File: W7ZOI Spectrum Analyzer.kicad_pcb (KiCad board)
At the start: 2 copper layers, 107.9 x 90.4 mm, 57 parts, among them J402 Jack-DC, J404 Jack-DC, J8 Conn_Coaxial, J9 Conn_Coaxial, U401 LM358, U402 LM358, U403 LM358

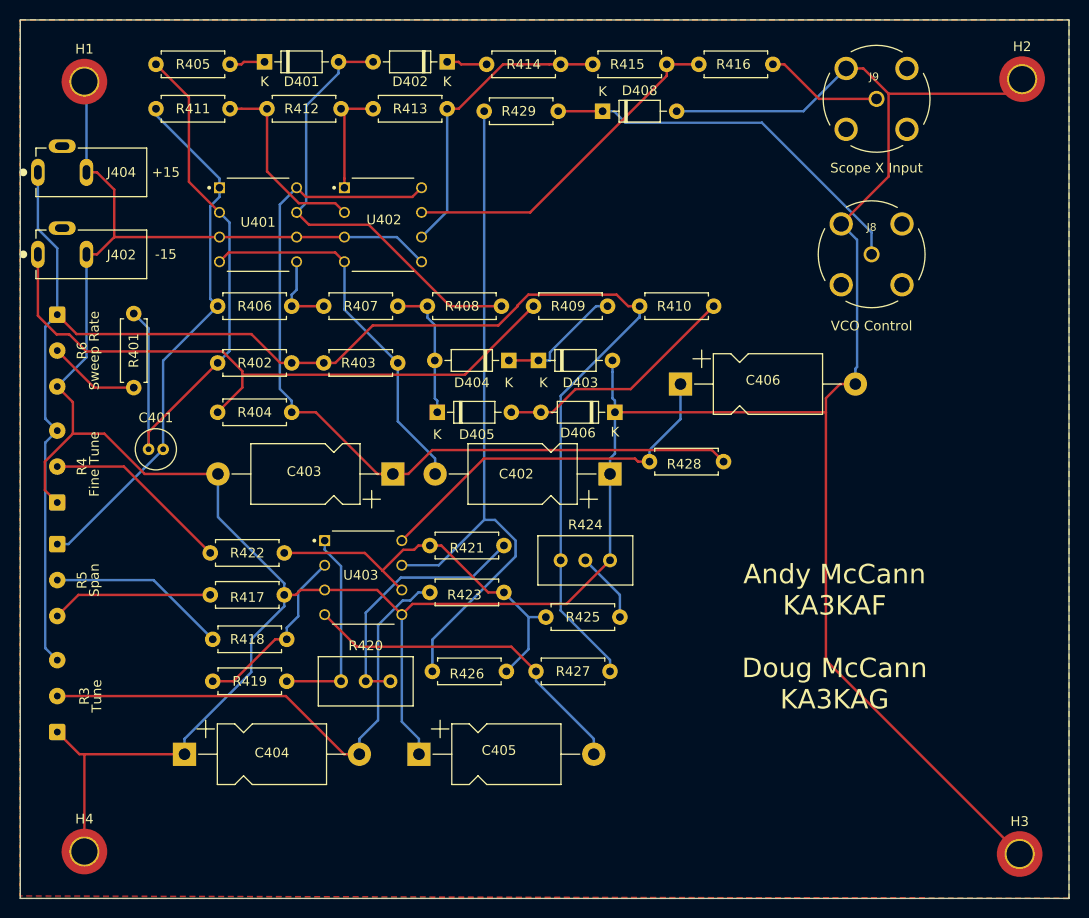
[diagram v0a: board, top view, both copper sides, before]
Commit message: Reduced size of timebase pcb
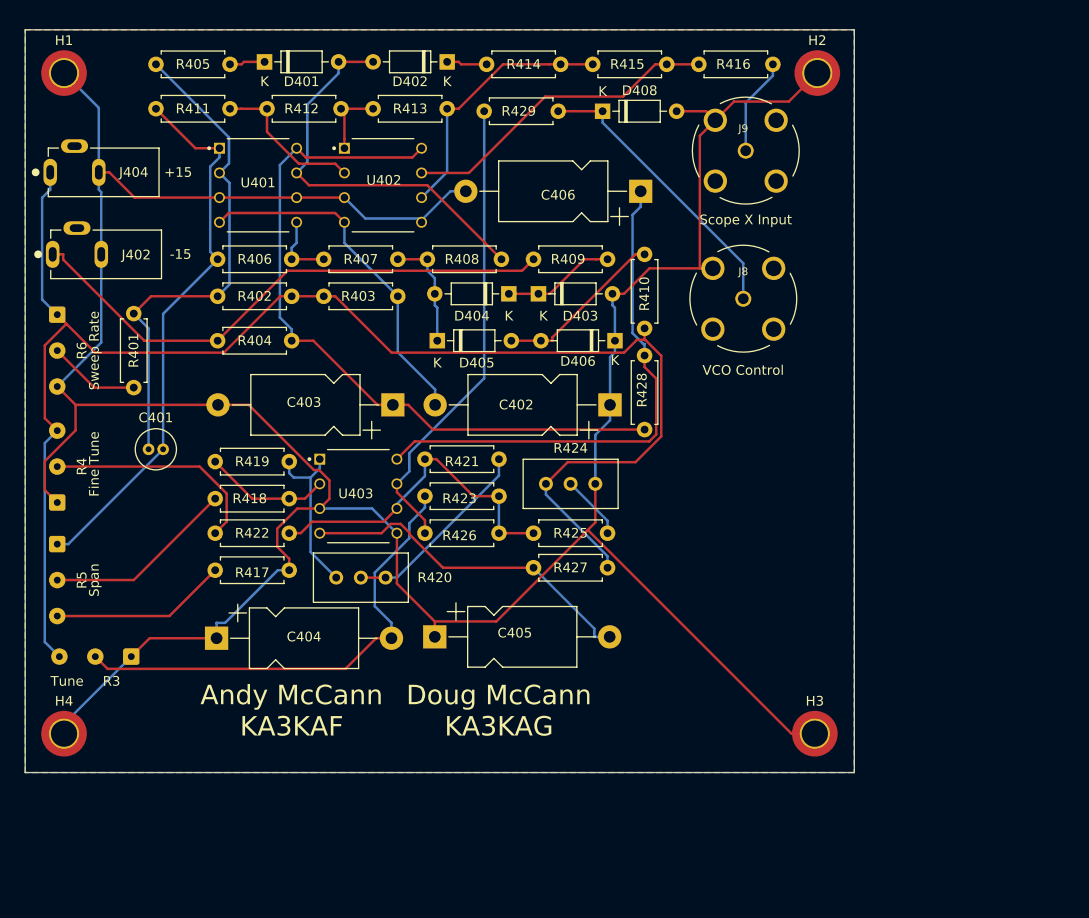
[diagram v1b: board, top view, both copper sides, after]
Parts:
- moved H3 24.4 mm to (132.1, 97.9)
- moved R419 22.6 mm to (70.4, 69.8)
- moved H2 21.1 mm to (132.3, 29.9)
- moved C406 20.3 mm to (114.2, 42.0), turned to 180 degrees
- moved R418 14.5 mm to (70.4, 73.7)
- moved J9 14.5 mm to (125.0, 37.8)
- moved R426 14.2 mm to (99.6, 77.2)
- moved J8 14.0 mm to (124.7, 53.1)
- moved C404 12.4 mm to (70.5, 88.0)
- moved H4 12.3 mm to (54.8, 97.9)
- moved C405 12.2 mm to (93.0, 87.9)
- moved R3 10.9 mm to (61.7, 89.9), turned to 180 degrees
- moved R420 10.7 mm to (87.9, 81.8)
- moved R427 10.7 mm to (103.1, 80.8)
- moved R423 9.92 mm to (99.6, 73.4)
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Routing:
- net GND: track 385.4 -> 308.7 mm
- net Net-(R426-Pad2): track 73.6 -> 48.4 mm
- net Net-(C406-Pad1): track 38.4 -> 54.2 mm
- net Net-(C403-Pad1): track 86.6 -> 74.8 mm
- net V+15: track 67.9 -> 57.0 mm
- net VCO_Out: track 39.7 -> 29.9 mm
- net Net-(C401-Pad1): track 60.8 -> 52.3 mm
- net Net-(D405-Pad2): track 25.4 -> 17.6 mm
- net Net-(R420-Pad1): track 26.7 -> 20.3 mm
- net Net-(R421-Pad2): track 41.2 -> 35.0 mm
- net Net-(R418-Pad2): track 18.6 -> 13.0 mm
- net V-15: track 161.6 -> 156.9 mm
- net Net-(C404-Pad2): track 54.4 -> 49.8 mm
- net Net-(D401-Pad2): track 45.9 -> 41.5 mm
- net Net-(R411-Pad2): track 20.0 -> 15.9 mm
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- added copper zone on B.Cu, net GND
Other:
- board size 107.9 x 90.4 mm -> 85.3 x 76.5 mm
- board text added: "Andy McCann KA3KAF"
- board text added: "Doug McCann KA3KAG"
- board text removed: "Andy McCann KA3KAF Doug McCann KA3KAG"
